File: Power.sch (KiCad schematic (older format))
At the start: 0 parts

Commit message: Module 3, Unit 6: Understanding The Power Protection And Filtering Module
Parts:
- added C? (x2): C, symbol C
- added F? (x4): FUSE, symbol FUSE
- added L? (x2): INDUCTOR, symbol INDUCTOR
- added P?: CONN_12X2, symbol CONN_12X2
- added R?: R, symbol R
- added SW?: SWITCH_INV, symbol SWITCH_INV
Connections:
- new net: F?.1, P?.10 (P10)
- new net: F?.1, P?.14 (P14)
- new net: P?.16 (P16), SW?.2
- new net: F?.1, P?.2 (P2)
- new net: F?.1, P?.4 (P4), P?.6 (P6)
- new net: R?.1, SW?.1
- new net +12P: F?.2, L?.1
- new net +12V: C?.1, L?.2
- new net +3.3V: F?.2, R?.2
- new net +5V: F?.2
- new net -12P: F?.2, L?.2
- new net -12V: C?.2, L?.1
- new net GND: C?.1, C?.2, P?.3 (P3), P?.5 (P5), SW?.3

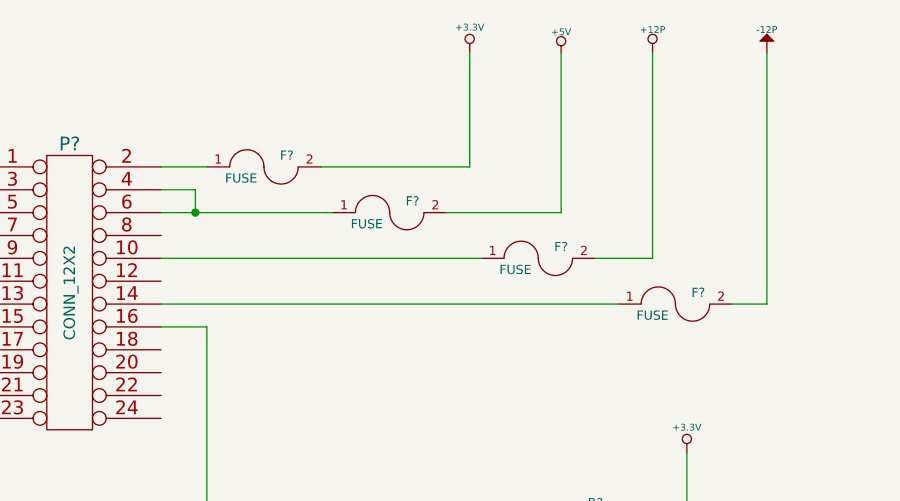
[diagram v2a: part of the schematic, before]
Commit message: Module 3, Unit 10: Revisiting The Current/Fan Module
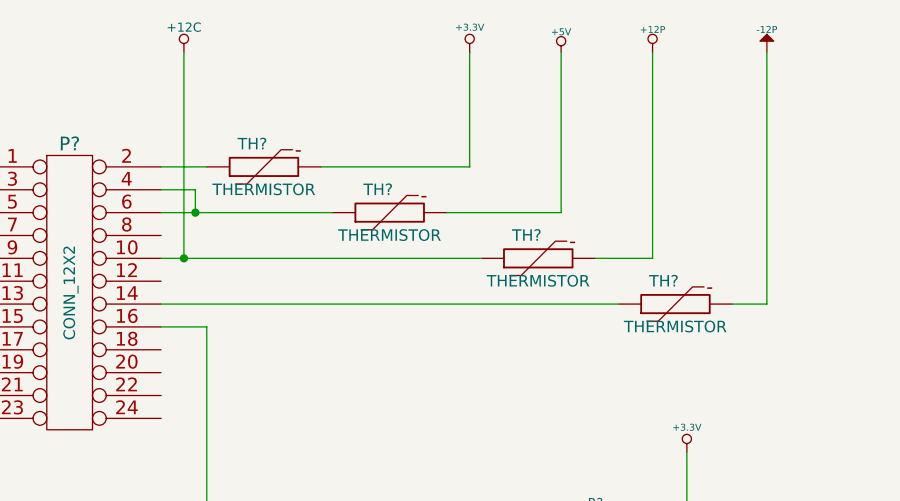
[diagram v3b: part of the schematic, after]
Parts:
- removed F? (x4): FUSE, symbol FUSE
- added TH? (x4): THERMISTOR, symbol THERMISTOR
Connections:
- net +12P: now also TH?.2
- net +3.3V: now also TH?.2
- net +5V: now also TH?.2
- net -12P: now also TH?.2
- net +12C: now reaches P?.10 (P10)
- net +12C: now also TH?.1
- net at P?.14 (P14): now also TH?.1
- net at P?.2 (P2): now also TH?.1
- net at P?.4 (P4), P?.6 (P6): now also TH?.1
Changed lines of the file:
@@
 $Descr A4 11693 8268
 encoding utf-8
-Sheet 5 9
+Sheet 4 9
 Title ""
 Date ""
@@
 $EndComp
 $Comp
-L FUSE F?
-U 1 1 53015314
-P 3300 1750
-F 0 "F?" H 3400 1800 40  0000 C CNN
-F 1 "FUSE" H 3200 1700 40  0000 C CNN
-F 2 "" H 3300 1750 60  0000 C CNN
-F 3 "" H 3300 1750 60  0000 C CNN
-	1    3300 1750
-	1    0    0    -1
-$EndComp
-$Comp
-L FUSE F?
-U 1 1 53015330
-P 3850 1950
-F 0 "F?" H 3950 2000 40  0000 C CNN
-F 1 "FUSE" H 3750 1900 40  0000 C CNN
-F 2 "" H 3850 1950 60  0000 C CNN
-F 3 "" H 3850 1950 60  0000 C CNN
-	1    3850 1950
-	1    0    0    -1
-$EndComp
-$Comp
-L FUSE F?
-U 1 1 5301533B
-P 4500 2150
-F 0 "F?" H 4600 2200 40  0000 C CNN
-F 1 "FUSE" H 4400 2100 40  0000 C CNN
-F 2 "" H 4500 2150 60  0000 C CNN
-F 3 "" H 4500 2150 60  0000 C CNN
-	1    4500 2150
-	1    0    0    -1
-$EndComp
-$Comp
-L FUSE F?
-U 1 1 53015346
-P 5100 2350
-F 0 "F?" H 5200 2400 40  0000 C CNN
-F 1 "FUSE" H 5000 2300 40  0000 C CNN
-F 2 "" H 5100 2350 60  0000 C CNN
-F 3 "" H 5100 2350 60  0000 C CNN
-	1    5100 2350
-	1    0    0    -1
-$EndComp
-$Comp
 L SWITCH_INV SW?
 U 1 1 53015353
@@
 	9350 2450 9350 2300
 Connection ~ 8750 2450
+Wire Wire Line
+	2950 2150 2950 1250
+Connection ~ 2950 2150
+$Comp
+L +12C #PWR?
+U 1 1 5302E7E0
+P 2950 1250
+F 0 "#PWR?" H 2950 1220 30  0001 C CNN
+F 1 "+12C" H 2950 1360 40  0000 C CNN
+F 2 "" H 2950 1250 60  0000 C CNN
+F 3 "" H 2950 1250 60  0000 C CNN
+	1    2950 1250
+	1    0    0    -1
+$EndComp
+$Comp
+L THERMISTOR TH?
+U 1 1 5302EABC
+P 3300 1750
+F 0 "TH?" V 3400 1800 50  0000 C CNN
+F 1 "THERMISTOR" V 3200 1750 50  0000 C CNN
+F 2 "" H 3300 1750 60  0000 C CNN
+F 3 "" H 3300 1750 60  0000 C CNN
+	1    3300 1750
+	0    -1   -1   0
+$EndComp
+$Comp
+L THERMISTOR TH?
+U 1 1 5302EAD3
+P 3850 1950
+F 0 "TH?" V 3950 2000 50  0000 C CNN
+F 1 "THERMISTOR" V 3750 1950 50  0000 C CNN
+F 2 "" H 3850 1950 60  0000 C CNN
+F 3 "" H 3850 1950 60  0000 C CNN
+	1    3850 1950
+	0    -1   -1   0
+$EndComp
+$Comp
+L THERMISTOR TH?
+U 1 1 5302EADE
+P 4500 2150
+F 0 "TH?" V 4600 2200 50  0000 C CNN
+F 1 "THERMISTOR" V 4400 2150 50  0000 C CNN
+F 2 "" H 4500 2150 60  0000 C CNN
+F 3 "" H 4500 2150 60  0000 C CNN
+	1    4500 2150
+	0    -1   -1   0
+$EndComp
+$Comp
+L THERMISTOR TH?
+U 1 1 5302EAE9
+P 5100 2350
+F 0 "TH?" V 5200 2400 50  0000 C CNN
+F 1 "THERMISTOR" V 5000 2350 50  0000 C CNN
+F 2 "" H 5100 2350 60  0000 C CNN
+F 3 "" H 5100 2350 60  0000 C CNN
+	1    5100 2350
+	0    -1   -1   0
+$EndComp
 $EndSCHEMATC
